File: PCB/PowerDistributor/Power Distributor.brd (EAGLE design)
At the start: 39.4 x 35.6 mm, 16 parts, among them J3 5.5x2.1mm Barrel

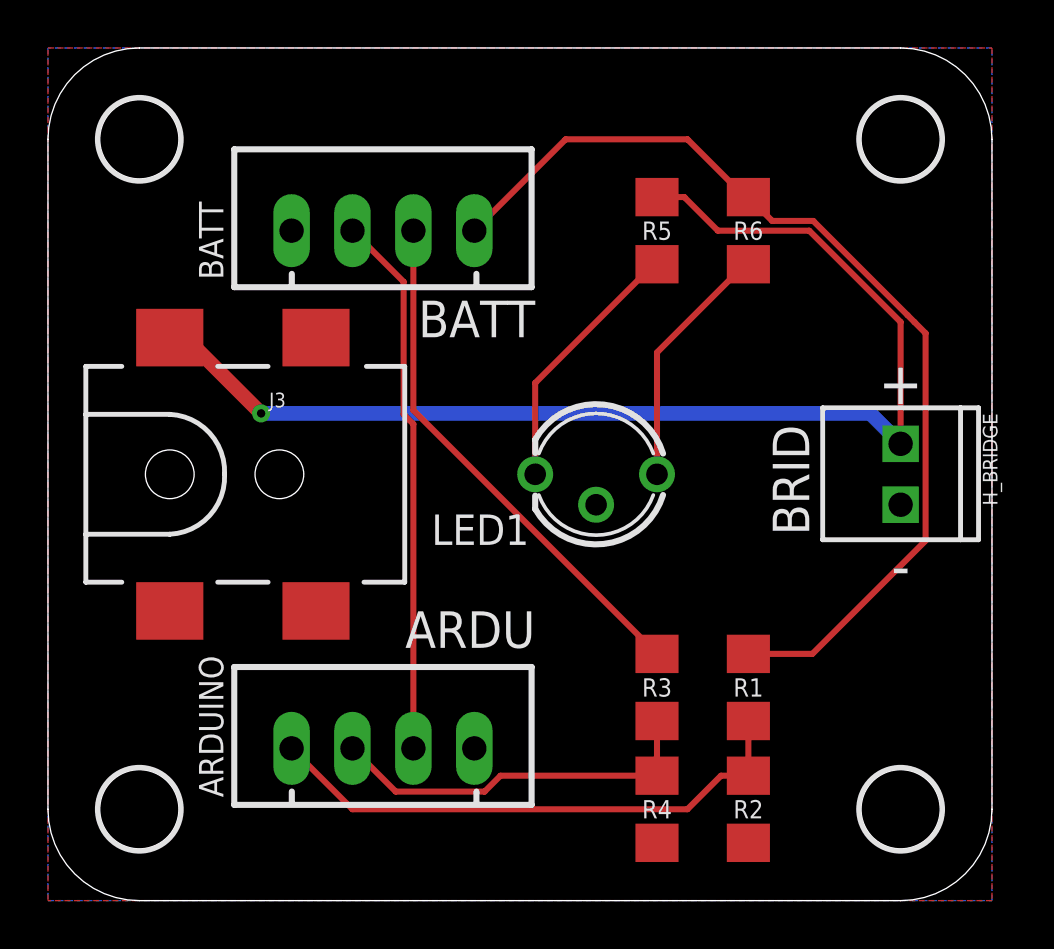
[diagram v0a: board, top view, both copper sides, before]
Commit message: update power distributor
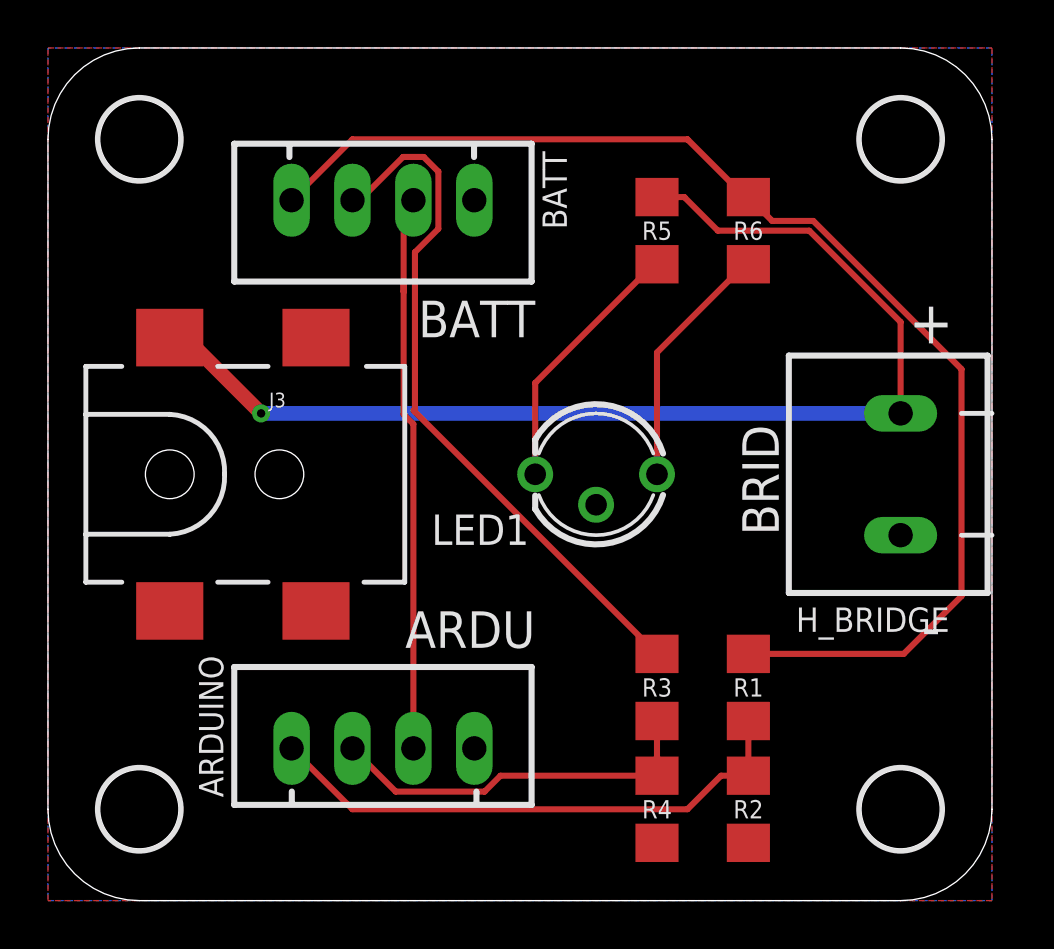
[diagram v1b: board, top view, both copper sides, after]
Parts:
- H_BRIDGE: value (none) -> SCREW-02; device SparkFun-Connectors:1X02_2.54_SCREWTERM -> KROBOT:SCREW-02
- moved BATT 7.73 mm to (17.8, 29.2), turned to 180 degrees
- moved H_BRIDGE 3.81 mm to (35.6, 15.2), turned to 90 degrees
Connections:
- net 12V: now also H_BRIDGE.2; no longer H_BRIDGE.P2
- net GND: now also H_BRIDGE.1; no longer H_BRIDGE.P1
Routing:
- net VDD: track 41.7 -> 52.3 mm
- net N$4: track 21.9 -> 29.4 mm
- net 12V: track 50.6 -> 48.8 mm
- net S1: track 22.6 -> 23.6 mm
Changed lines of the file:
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@@
 <layer number="21" name="tPlace" color="7" fill="1" visible="yes" active="yes"/>
 <layer number="22" name="bPlace" color="7" fill="1" visible="no" active="yes"/>
-<layer number="23" name="tOrigins" color="15" fill="1" visible="no" active="yes"/>
+<layer number="23" name="tOrigins" color="15" fill="1" visible="yes" active="yes"/>
 <layer number="24" name="bOrigins" color="15" fill="1" visible="no" active="yes"/>
 <layer number="25" name="tNames" color="7" fill="1" visible="no" active="yes"/>
@@
 <text x="20.32" y="25.019" size="1.524" layer="21" rot="R180">BATT</text>
 <text x="20.32" y="10.541" size="1.524" layer="21" rot="R180" align="top-left">ARDU</text>
-<text x="31.75" y="15.24" size="1.524" layer="21" rot="R90">BRID</text>
+<text x="30.48" y="15.24" size="1.524" layer="21" rot="R90">BRID</text>
 <text x="30.48" y="17.78" size="1.016" layer="22" rot="SMR270" align="center">Power Distributor v2.0 - KBOT
 2017 - Y. LABBE &amp; O. LEVEQUE</text>
-<text x="35.56" y="21.59" size="1.778" layer="21" align="center">+</text>
-<text x="35.56" y="13.97" size="1.778" layer="21" align="center">-</text>
+<text x="36.83" y="24.13" size="1.778" layer="21" align="center">+</text>
+<text x="36.83" y="11.43" size="1.778" layer="21" align="center">-</text>
 <dimension x1="3.81" y1="31.75" x2="3.81" y2="3.81" x3="-7.62" y3="17.78" textsize="1.778" layer="47"/>
 <dimension x1="3.81" y1="31.75" x2="35.56" y2="31.75" x3="19.685" y3="41.91" textsize="1.778" layer="47"/>
@@
 </autorouter>
 <elements>
-<element name="BATT" library="KROBOT" package="JST-XH-04-PACKAGE-LONG-PAD" value="JST-XH-04-PIN-LONG-PAD" x="10.16" y="27.94"/>
-<element name="H_BRIDGE" library="SparkFun-Connectors" package="1X02_2.54_SCREWTERM" value="" x="35.56" y="19.05" rot="R270"/>
+<element name="BATT" library="KROBOT" package="JST-XH-04-PACKAGE-LONG-PAD" value="JST-XH-04-PIN-LONG-PAD" x="17.78" y="29.21" rot="R180"/>
+<element name="H_BRIDGE" library="KROBOT" package="SCREW-02" value="SCREW-02" x="35.56" y="15.24" rot="R90"/>
 <element name="J3" library="SparkFun-Connectors" package="POWER_JACK_SMD" value="5.5x2.1mm Barrel" x="5.08" y="17.78">
 <attribute name="PROD_ID" value="CONN-08106" x="5.08" y="17.78" size="1.778" layer="27" display="off"/>
@@
 <contactref element="J3" pad="GND"/>
 <contactref element="J3" pad="P$4"/>
-<contactref element="H_BRIDGE" pad="P1"/>
+<contactref element="H_BRIDGE" pad="1"/>
 <contactref element="LED1" pad="CC"/>
 <contactref element="BATT" pad="1"/>
@@
 <wire x1="29.21" y1="29.34" x2="29.08" y2="29.34" width="0.254" layer="1"/>
 <wire x1="29.08" y1="29.34" x2="26.67" y2="31.75" width="0.254" layer="1"/>
-<wire x1="26.67" y1="31.75" x2="21.59" y2="31.75" width="0.254" layer="1"/>
-<wire x1="21.59" y1="31.75" x2="17.78" y2="27.94" width="0.254" layer="1"/>
-<wire x1="29.21" y1="10.29" x2="31.88" y2="10.29" width="0.254" layer="1"/>
-<wire x1="36.6014" y1="15.0114" x2="31.88" y2="10.29" width="0.254" layer="1"/>
 <wire x1="30.2036" y1="28.3464" x2="29.21" y2="29.34" width="0.254" layer="1"/>
 <wire x1="31.9183375" y1="28.3464" x2="30.2036" y2="28.3464" width="0.254" layer="1"/>
-<wire x1="36.1347375" y1="24.13" x2="35.84736875" y2="24.41736875" width="0.254" layer="1"/>
-<wire x1="35.84736875" y1="24.41736875" x2="31.9183375" y2="28.3464" width="0.254" layer="1"/>
-<wire x1="36.1347375" y1="24.13" x2="36.6014" y2="23.6633375" width="0.254" layer="1"/>
-<wire x1="36.6014" y1="23.6633375" x2="36.6014" y2="15.0114" width="0.254" layer="1"/>
+<wire x1="31.9183375" y1="28.3464" x2="38.1" y2="22.1647375" width="0.254" layer="1"/>
+<wire x1="38.1" y1="22.1647375" x2="38.1" y2="12.7" width="0.254" layer="1"/>
+<wire x1="38.1" y1="12.7" x2="35.69" y2="10.29" width="0.254" layer="1"/>
+<wire x1="35.69" y1="10.29" x2="29.21" y2="10.29" width="0.254" layer="1"/>
+<wire x1="12.7" y1="31.75" x2="10.16" y2="29.21" width="0.254" layer="1"/>
+<wire x1="26.67" y1="31.75" x2="12.7" y2="31.75" width="0.254" layer="1"/>
 </signal>
 <signal name="12V">
 <contactref element="J3" pad="VIN0"/>
-<contactref element="H_BRIDGE" pad="P2"/>
+<contactref element="H_BRIDGE" pad="2"/>
 <contactref element="R5" pad="2"/>
 <wire x1="5.08" y1="24.13" x2="8.89" y2="20.32" width="0.6096" layer="1"/>
 <wire x1="5.08" y1="24.13" x2="5.08" y2="23.48" width="0.6096" layer="1"/>
 <via x="8.89" y="20.32" extent="1-16" drill="0.35"/>
-<wire x1="8.89" y1="20.32" x2="34.29" y2="20.32" width="0.6096" layer="16"/>
-<wire x1="34.29" y1="20.32" x2="35.56" y2="19.05" width="0.6096" layer="16"/>
 <wire x1="25.4" y1="29.34" x2="26.54" y2="29.34" width="0.254" layer="1"/>
 <wire x1="26.54" y1="29.34" x2="27.94" y2="27.94" width="0.254" layer="1"/>
 <wire x1="27.94" y1="27.94" x2="31.75" y2="27.94" width="0.254" layer="1"/>
 <wire x1="31.75" y1="27.94" x2="35.56" y2="24.13" width="0.254" layer="1"/>
-<wire x1="35.56" y1="24.13" x2="35.56" y2="19.05" width="0.254" layer="1"/>
+<wire x1="35.56" y1="24.13" x2="35.56" y2="20.32" width="0.254" layer="1"/>
+<wire x1="35.56" y1="20.32" x2="8.89" y2="20.32" width="0.6096" layer="16"/>
 </signal>
 <signal name="N$9">
@@
 <contactref element="ARDUINO" pad="3"/>
 <wire x1="15.24" y1="6.35" x2="15.24" y2="19.8752625" width="0.254" layer="1"/>
-<wire x1="14.8336" y1="25.8064" x2="12.7" y2="27.94" width="0.254" layer="1"/>
 <wire x1="15.24" y1="19.8752625" x2="14.8336" y2="20.2816625" width="0.254" layer="1"/>
-<wire x1="14.8336" y1="20.2816625" x2="14.8336" y2="25.8064" width="0.254" layer="1"/>
+<wire x1="14.8336" y1="20.2816625" x2="14.8336" y2="25.4" width="0.254" layer="1"/>
+<wire x1="14.8336" y1="25.4" x2="14.8336" y2="25.8064" width="0.254" layer="1"/>
+<wire x1="14.8336" y1="25.4" x2="14.8336" y2="28.8036" width="0.254" layer="1"/>
+<wire x1="14.8336" y1="28.8036" x2="15.24" y2="29.21" width="0.254" layer="1"/>
 </signal>
 <signal name="N$4">
 <contactref element="BATT" pad="3"/>
 <contactref element="R3" pad="1"/>
-<wire x1="15.24" y1="27.94" x2="15.24" y2="20.45" width="0.254" layer="1"/>
-<wire x1="15.24" y1="20.45" x2="25.4" y2="10.29" width="0.254" layer="1"/>
+<wire x1="15.24" y1="20.45" x2="15.305" y2="20.385" width="0.254" layer="1"/>
+<wire x1="15.305" y1="20.385" x2="25.4" y2="10.29" width="0.254" layer="1"/>
+<wire x1="16.2814" y1="28.0166375" x2="16.2814" y2="30.4033625" width="0.254" layer="1"/>
+<wire x1="16.2814" y1="30.4033625" x2="15.6713625" y2="31.0134" width="0.254" layer="1"/>
+<wire x1="15.6713625" y1="31.0134" x2="14.8086375" y2="31.0134" width="0.254" layer="1"/>
+<wire x1="15.305" y1="27.0402375" x2="16.2814" y2="28.0166375" width="0.254" layer="1"/>
+<wire x1="15.305" y1="20.385" x2="15.305" y2="27.0402375" width="0.254" layer="1"/>
+<wire x1="13.0052375" y1="29.21" x2="12.7" y2="29.21" width="0.254" layer="1"/>
+<wire x1="14.8086375" y1="31.0134" x2="13.0052375" y2="29.21" width="0.254" layer="1"/>
 </signal>
 <signal name="S3">
